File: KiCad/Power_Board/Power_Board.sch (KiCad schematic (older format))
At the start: 19 parts, among them U1 AD1583, U2 MAX5259, U3 MAX5259

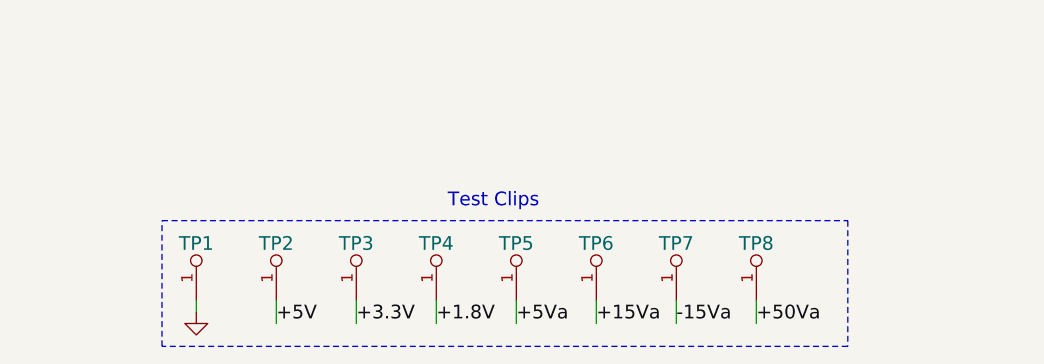
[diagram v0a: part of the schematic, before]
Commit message: Added a Vin test clip.
Also did a bit of copper pour cutout cleanup.
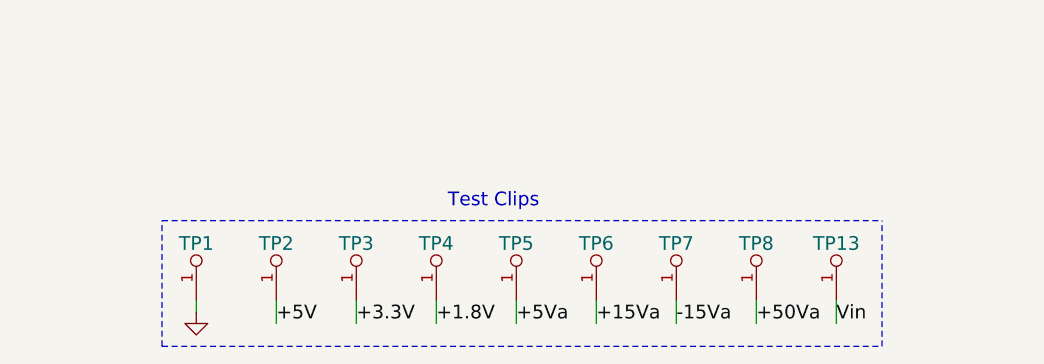
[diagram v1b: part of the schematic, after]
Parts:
- added TP13: Test_Point, OpenCamera:TEST_CLIP, symbol Test_Point
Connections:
- net Vin: now also TP13.1
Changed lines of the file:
@@
 	1950 7350 1950 7400
 Wire Notes Line
-	1800 7000 4800 7000
+	1800 7000 4950 7000
 Wire Notes Line
-	4800 7000 4800 7550
-Wire Notes Line
-	4800 7550 1800 7550
+	1800 7550 4950 7550
 Wire Notes Line
 	1800 7550 1800 7000
@@
 Wire Wire Line
 	9150 4550 9250 4550
+$Comp
+L Test_Point TP13
+U 1 1 5599F567
+P 4750 7350
+F 0 "TP13" H 4750 7600 60  0000 C CNN
+F 1 "Test_Point" H 4750 7700 60  0001 C CNN
+F 2 "OpenCamera:TEST_CLIP" H 4750 7350 60  0001 C CNN
+F 3 "" H 4750 7350 60  0000 C CNN
+	1    4750 7350
+	1    0    0    -1
+$EndComp
+Text Label 4750 7450 0    60   ~ 0
+Vin
+Wire Wire Line
+	4750 7350 4750 7450
+Wire Notes Line
+	4950 7550 4950 7000
 $EndSCHEMATC

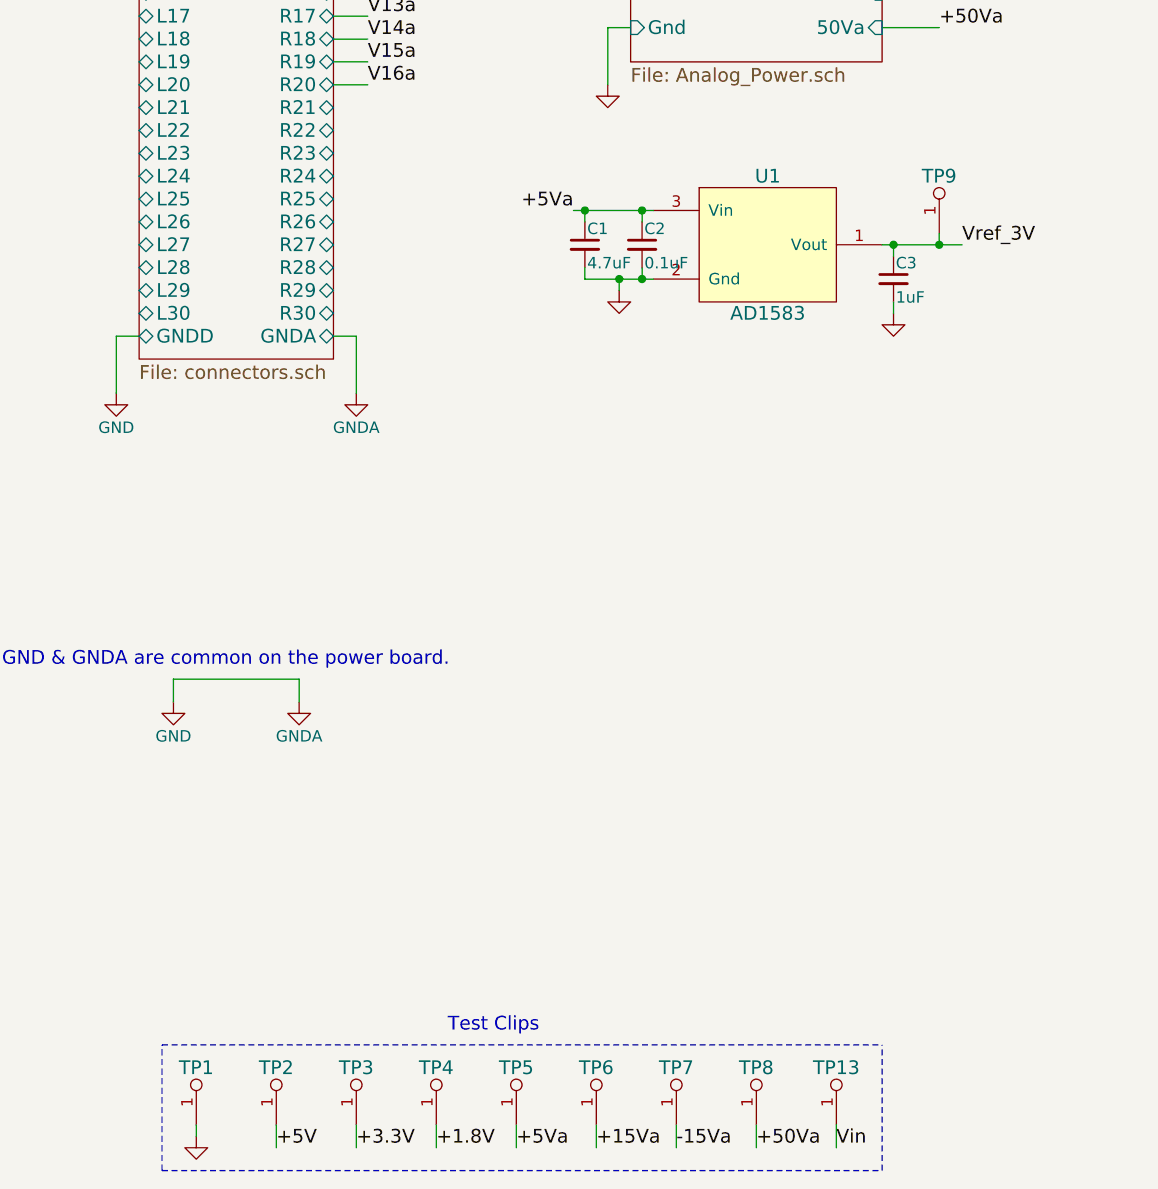
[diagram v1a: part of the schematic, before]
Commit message: Component changes
Switched Vref test point to test clip.
Beefed up 0ohm jumpers to 0805.
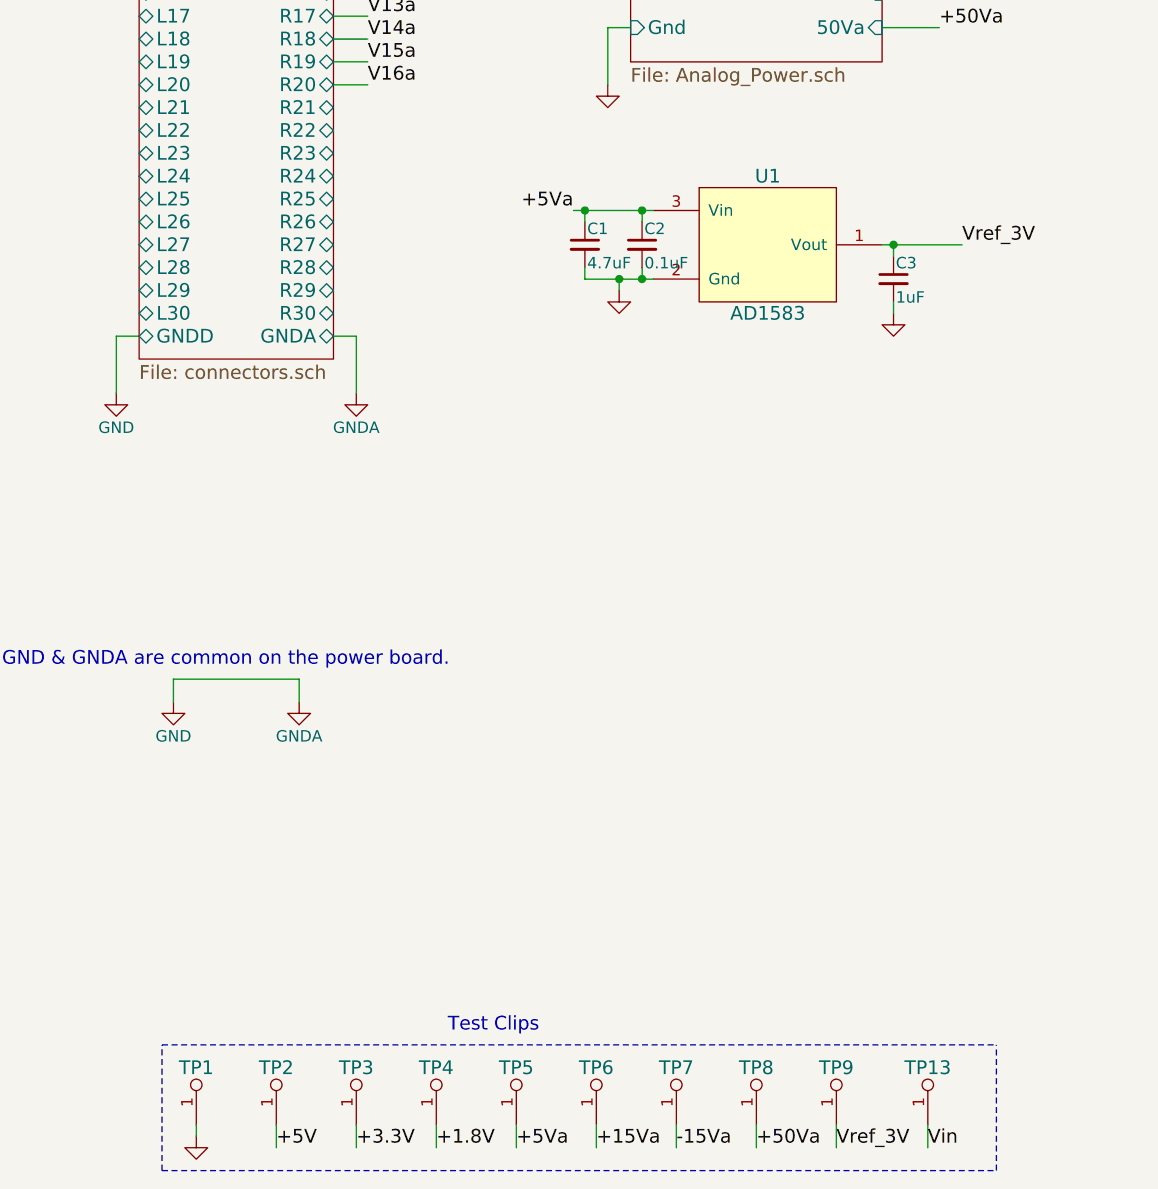
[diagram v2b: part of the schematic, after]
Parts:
- TP9: footprint OpenCamera:TEST_POINT_SMD -> OpenCamera:TEST_CLIP
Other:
- moved on the sheet: TP13, TP9
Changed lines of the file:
@@
 Sheet 1 4
 Title "Power Board"
-Date "Sunday, July 05, 2015"
+Date "Monday, July 06, 2015"
 Rev "1.1"
 Comp "Open Camera Project"
@@
 L Test_Point TP9
 U 1 1 55928CD4
-P 5200 3450
-F 0 "TP9" H 5200 3700 60  0000 C CNN
-F 1 "Test_Point" H 5200 3800 60  0001 C CNN
-F 2 "OpenCamera:TEST_POINT_SMD" H 5200 3450 60  0001 C CNN
-F 3 "" H 5200 3450 60  0000 C CNN
-	1    5200 3450
+P 4750 7350
+F 0 "TP9" H 4750 7600 60  0000 C CNN
+F 1 "Test_Point" H 4750 7700 60  0001 C CNN
+F 2 "OpenCamera:TEST_CLIP" H 4750 7350 60  0001 C CNN
+F 3 "" H 4750 7350 60  0000 C CNN
+	1    4750 7350
 	1    0    0    -1
 $EndComp
@@
 	3700 7350 3700 7450
 Wire Wire Line
-	5200 3450 5200 3500
-Connection ~ 5200 3500
-Wire Wire Line
 	4400 7350 4400 7450
 Wire Wire Line
 	1950 7350 1950 7400
 Wire Notes Line
-	1800 7000 4950 7000
+	1800 7000 5450 7000
 Wire Notes Line
-	1800 7550 4950 7550
+	1800 7550 5450 7550
 Wire Notes Line
 	1800 7550 1800 7000
@@
 L Test_Point TP13
 U 1 1 5599F567
-P 4750 7350
-F 0 "TP13" H 4750 7600 60  0000 C CNN
-F 1 "Test_Point" H 4750 7700 60  0001 C CNN
-F 2 "OpenCamera:TEST_CLIP" H 4750 7350 60  0001 C CNN
-F 3 "" H 4750 7350 60  0000 C CNN
-	1    4750 7350
-	1    0    0    -1
-$EndComp
+P 5150 7350
+F 0 "TP13" H 5150 7600 60  0000 C CNN
+F 1 "Test_Point" H 5150 7700 60  0001 C CNN
+F 2 "OpenCamera:TEST_CLIP" H 5150 7350 60  0001 C CNN
+F 3 "" H 5150 7350 60  0000 C CNN
+	1    5150 7350
+	1    0    0    -1
+$EndComp
+Text Label 5150 7450 0    60   ~ 0
+Vin
+Wire Wire Line
+	5150 7350 5150 7450
 Text Label 4750 7450 0    60   ~ 0
-Vin
+Vref_3V
 Wire Wire Line
 	4750 7350 4750 7450
 Wire Notes Line
-	4950 7550 4950 7000
+	5450 7550 5450 7000
 $EndSCHEMATC
